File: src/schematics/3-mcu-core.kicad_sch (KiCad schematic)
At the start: 42 parts, among them U301 PIC32CX1025SG41100T-I/E5X

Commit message: Further MCU elaboration and pin mapping.
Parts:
- added R12, R13, R3??, R3ca-3cb, R3cb: ??Ω, restall-generic-resistors:nominal-0402-1005, symbol restall-generic-resistors:resistor
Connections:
- net SWCLK: now also U301.60 (PC20)
- net SWDIO: now also U301.61 (PC21)
- net TFT_SEL: now also U301.41 (PC11)
- net ~{RESET}: now also U301.58 (PC18)
- net ~{SDCARD_BUSYLED}: now also U301.81 (PB25); no longer CONN5.2 (P2)
- net ~{TFT_RESET}: now also U301.40 (PC10)
- net MSF_OUT_{+}: now reaches U301.15 (PB08)
- net MSF_OUT_{-}: now reaches U301.16 (PB09)
- net AMP_IN: now reaches U301.18 (PA05)
- net SHCP: now reaches U301.21 (PC05)
- net STCP: now reaches U301.22 (PC06)
- net DS: now reaches U301.23 (PC07)
- net at U301.26 (PA08): now also R3ca-3cb.2
- net at U301.27 (PA09): now also R12.2
- net at U301.28 (PA10): now also R13.2
- net at U301.29 (PA11): now also R3cb.2
- net AMP_EN: now reaches U301.3 (PC00)
- net at U301.32 (PB10): now also R3??.2
- net ~{SS}: now reaches U301.33 (PB11)
- net TFT_TEAR0: now reaches U301.34 (PB12)
- net TFT_TEAR1: now reaches U301.35 (PB13)
- net TFT_TP_INT0: now reaches U301.36 (PB14)
- net TFT_TP_INT1: now reaches U301.37 (PB15)
- net MSF_REC_EN: now reaches U301.4 (PC01)
- net D_{-}: now reaches U301.74 (PA24)
- net D_{+}: now reaches U301.75 (PA25)
- new net DATA0: R3ca-3cb.1
- new net DATA1: R12.1
- new net DATA2: R13.1
- new net DATA3: R3cb.1
- new net SCK: R3??.1
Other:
- note added: "TODO: BUSYLED WANTS A MOSFET / BJT - LESS INSTANTANEOUS CURRENT FLOWING THROUGH MCU'S VSS."
- note added: "TODO: CAPACITOR(S) ?"
- note added: "TODO: FIG9.4 / P28 of PIC32 Troubleshooting - example of SWD ESD / pull-ups"
- note added: "TODO: GND, PREFERABLY - OR GND THROUGH R. KEEPS NOISE FROM OSCILLATOR (JITTER). STATIC DIGITAL I/O FINE TOO - LIKE USB_SUSPEND MAYBE ?"
- note added: "TODO: NEED PULL-UPS OR ANYTHING ON THE DEBUG PINS ? SWCLK NEEDS 1k PULL-UP POSSIBLY ESD PROTECTION AT ALL CONNECTORS"
- note added: "TODO: P5-P20 are INPUT ONLY"
- note added: "TODO: PB0-3 = gnd ideally"
- note added: "TODO: PULL-UPS OR PULL-DOWNS ON TFT_TEAR* AND TFT_INT* ? IN CASE THE CONNECTOR POPS OUT. MAYBE JUST USE INTERNAL ONES ?"
- note added: "TODO: SPI - SERCOM: PAD1 IS CLK PAD2 IS SS (ONLY USED IN SLAVE MODE - SO TIE THIS TO ~{RESET}) PAD0 OR PAD3 IS DATA OUT PAD3 OR PAD0 IS DATA IN UART: TX=PAD0, RX=PAD1(OR SCK IF SYNC, THEN RX=PAD0), CTS=PAD3, RTS=PAD2"
- note added: "TODO: SPI.~{SS} NEEDS A PULL-UP TO VDD - BUT IT ALREADY WILL HAVE ONE SINCE IT'S SHARED WITH THE RESET..."
- note added: "TODO: SWCLK / SWDIO - NEED SERIES TERMINATORS..."
- note added: "TODO: THE SPI.~{SS} PAD IS REQUIRED BY THE BC805M SLAVE - THIS MEANS THE RESET PIN MUST BE USED AS A GPIO."
- note added: "TODO: THESE NETS NEED SUPPLIES / CIRCUITRY"
- note added: "TODO: UART RX FOR IR RECEIVER"
- note added: "TODO: series terminators, subtract 4.5ohms for switch resistance"
- note added: "TODO: ~{RESET} NEEDS TO BE SHARED...WON'T BE A DIRECT DEBUG BUS CONNECTION. WILL ALSO WANT A PULL-UP, CAPACITOR, ETC. A PUSH-BUTTON ALSO (BUTTON IN ROOT SCHEMATIC; ADD HIERARCHY PIN)"
- note added: "x BLE_DEBUG = 2 pins + 2o x MSF GAIN CONTROL = 3 pins + 3o x MSF POWER = 1 pin + 1o USB POWER FAULT = 1 pin + USB FUSB INT = 1 pin + USB BC DETECT = 3 pins + USB SUSPEND OUTPUT = 1 pin + 1o SD CARD POWER = 1 pin + 1o x AUDIO POWER = 1 pin + 1o HUMIDITY = 1 pin (optionally 2 pins) + PROXIMITY = 2 pins + PRESSURE = 1 pin = 19 pins ! (9 outputs)"
- note removed: "TODO: IR UART (CHECK SERCOM PINS !) MAYBE EVEN ANOTHER PERIPHERAL LIKE TCC ? AND THEN THIS SERCOM CAN BE USED FOR THE BC805M SWD. SERCOM5 (P99 & P100) MIGHT BE BETTER FOR IR LED. ALSO CONSIDER 'WAKE UP' - SERCOM NEEDS CLOCKING TO OPERATE IN SLEEP (TOO MUCH CURRENT FOR USB SUSPEND)"
- note removed: "TODO: NEED PULL-UPS OR ANYTHING ON THE DEBUG PINS ?"
- note removed: "TODO: SPEAKER"
- note removed: "TODO: SPI - SERCOM: PAD1 IS CLK PAD2 IS SS PAD0 OR PAD3 IS DATA OUT PAD3 OR PAD0 IS DATA IN UART: TX, RX, CTS, RTS"
- note removed: "TODO: SPI.~{SS} NEEDS A PULL-UP TO VDD"
- note removed: "TODO: ~{RESET} NEEDS TO BE SHARED...WON'T BE A DIRECT DEBUG BUS CONNECTION."
- moved on the sheet: C14, C15, C16, C17, C301, C302, R1, R2, R301, XTAL301, XTAL302, XTAL303

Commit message: Further elaboration of the design, particularly around the power budget.  It's clear that the USB Suspend current of 2.5mA won't be met, mainly due to the DPS1133 power switch's quiescent current.  This is a nice part worth keeping though as it contains OVP, OCP and reverse voltage protection all in one, up to 24V maximum input.
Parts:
- added Q1: MMBT3904, restall-manufacturer-diodes-inc:SOT-23, symbol restall-manufacturer-diodes-inc:MMBT3904
- added R2: 3.3kΩ, restall-generic-resistors:nominal-0402-1005, symbol restall-generic-resistors:resistor
- added R304, R305: 1.8kΩ, restall-generic-resistors:nominal-0402-1005, symbol restall-generic-resistors:resistor
- renumbered R1 to R302, R2 to R303
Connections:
- net GND: now also Q1.2 (E)
- net MCU_V{DD}: now also R304.1, R305.1
- net ~{SDCARD_BUSYLED}: now also Q1.3 (C); no longer U301.81 (PB25)
- net SDA: now reaches U301.72 (PA22)
- net SDA: now also R304.2
- net SCL: now reaches U301.73 (PA23)
- net SCL: now also R305.2
- new net: R2.1, U301.81 (PB25)
- new net: Q1.1 (B), R2.2
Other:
- note added: "Fast-Mode I^{2}C (400kHz)"
- note removed: "I2C SDA (P72 / PAD0) AND SCL (P73 / PAD1)"
- note removed: "TODO: BUSYLED WANTS A MOSFET / BJT - LESS INSTANTANEOUS CURRENT FLOWING THROUGH MCU'S VSS."

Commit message: Elaboration of the top-level schematicd.
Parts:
- added R3bb1, R3xx: ??Ω, restall-generic-resistors:nominal-0402-1005, symbol restall-generic-resistors:resistor
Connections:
- net SWCLK: now also R3bb1.2; no longer U301.60 (PC20)
- net SWDIO: now also R3xx.2; no longer U301.61 (PC21)
- net CD renamed ~{CD}
- net MSF_REC_EN renamed MSF_RCV_EN
- net WP renamed ~{WP}
- new net: R3bb1.1, U301.60 (PC20)
- new net: R3xx.1, U301.61 (PC21)
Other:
- note added: "R3??-??"
- note added: "TODO: ABOUT 330 ohms - less about Z matching, more about isolating from connector / debugger"
- note added: "TODO: ALREADY GOT THE BACKLIGHT SOMEWHERE ?"
- note added: "TODO: NOTE ABOUT ALL R AND C BEING 0402 UNLESS SPECIFIED. ALSO ALL R THICK FILM 1% 100ppm. ALSO ALL C MLCC +/- 10% X5R 16V."
- note added: "TODO: RESET NEEDS TO BE: MCU -> SERIES R -> R (PULL-UP) AND C TO GND -> BUS Verify signal levels at BC805M side. Verify rise time for when using the pin as ~{SPI.SS}."
- note removed: "TODO: NOTE ABOUT ALL R AND C BEING 0402 UNLESS SPECIFIED. ALSO ALL R THICK FILM 1% 100ppm. ALSO ALL C MLCC +/- 10% X7R 10V."
- note removed: "TODO: SWCLK / SWDIO - NEED SERIES TERMINATORS..."

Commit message: Further elaboration of the design and schematics, mainly power supply calculations.
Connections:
- net MCU_V{DD} renamed CORE_VDD_{+3.3V}
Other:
- note added: "TODO: NOTE ABOUT ALL R AND C BEING 0402 UNLESS SPECIFIED. ALSO ALL R THICK FILM 1% 100ppm. ALSO ALL C MLCC +/- 10% X5R 10V."
- note removed: "TODO: NOTE ABOUT ALL R AND C BEING 0402 UNLESS SPECIFIED. ALSO ALL R THICK FILM 1% 100ppm. ALSO ALL C MLCC +/- 10% X5R 16V."
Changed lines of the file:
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@@
     (effects (font (size 1.27 1.27)) (justify left bottom))
   )
-  (text "TODO: NOTE ABOUT ALL R AND C BEING 0402 UNLESS SPECIFIED.\nALSO ALL R THICK FILM 1% 100ppm.\nALSO ALL C MLCC +/- 10% X5R 16V."
+  (text "TODO: NOTE ABOUT ALL R AND C BEING 0402 UNLESS SPECIFIED.\nALSO ALL R THICK FILM 1% 100ppm.\nALSO ALL C MLCC +/- 10% X5R 10V."
     (at 309.372 261.874 0)
     (effects (font (size 1.27 1.27)) (justify left bottom))
@@
     (effects (font (size 1.27 1.27)) (justify right))
   )
+  (hierarchical_label "CORE_VDD_MODE" (shape output) (at 305.054 228.854 0) (fields_autoplaced)
+    (effects (font (size 1.27 1.27)) (justify left))
+  )
   (hierarchical_label "{MCU_DEBUG}" (shape bidirectional) (at 137.16 86.36 180) (fields_autoplaced)
     (effects (font (size 1.27 1.27)) (justify right))
@@
     (effects (font (size 1.27 1.27)) (justify left))
   )
-  (hierarchical_label "MCU_V{DD}" (shape output) (at 355.6 81.28 0) (fields_autoplaced)
+  (hierarchical_label "CORE_VDD_{+3.3V}" (shape input) (at 355.6 81.28 0) (fields_autoplaced)
     (effects (font (size 1.27 1.27)) (justify left))
   )
@@
           (reference "R2") (unit 1)
         )
-        (path "/56d623d3-22db-4d43-a9d9-e6bb4bb68946"
-          (reference "R001") (unit 1)
-        )
-        (path "/56d623d3-22db-4d43-a9d9-e6bb4bb68946/f496ae57-4ed4-47d4-8c97-f77f6741aea7"
-          (reference "R501") (unit 1)
-        )
       )
     )
@@
           (reference "R304") (unit 1)
         )
-        (path "/56d623d3-22db-4d43-a9d9-e6bb4bb68946"
-          (reference "R001") (unit 1)
-        )
-        (path "/56d623d3-22db-4d43-a9d9-e6bb4bb68946/f496ae57-4ed4-47d4-8c97-f77f6741aea7"
-          (reference "R501") (unit 1)
-        )
       )
     )
@@
           (reference "R305") (unit 1)
         )
-        (path "/56d623d3-22db-4d43-a9d9-e6bb4bb68946"
-          (reference "R001") (unit 1)
-        )
-        (path "/56d623d3-22db-4d43-a9d9-e6bb4bb68946/f496ae57-4ed4-47d4-8c97-f77f6741aea7"
-          (reference "R501") (unit 1)
-        )
-      )
+      )

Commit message: Started to draw the USB / power input module.
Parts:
- removed FB1: >600R @ 100MHz, symbol restall-generic-inductors:ferrite-bead
- added FB301: WLBD2012HCU601TH, restall-manufacturer-walsin:WLBD2012, symbol restall-manufacturer-walsin:WLBD2012HCU601TH
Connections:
- net CORE_VDD_{+3.3V}: now also FB301.1 (P1)
- net MCU_AV_{DD}: now also FB301.2 (P2)
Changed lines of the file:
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@@
     (stroke (width 0) (type default))
   )
+  (wire (pts (xy 71.12 101.6) (xy 76.2 101.6))
+    (stroke (width 0) (type default))
+  )
   (wire (pts (xy 132.08 238.76) (xy 139.7 238.76))
     (stroke (width 0) (type default))
@@
     (stroke (width 0) (type default))
   )
-  (wire (pts (xy 71.12 101.6) (xy 76.2 101.6))
-    (stroke (width 0) (type default))
-  )
   (wire (pts (xy 219.71 144.78) (xy 227.33 144.78))
     (stroke (width 0) (type default))
@@
     )
   )
-  (symbol (lib_id "restall-generic-inductors:ferrite-bead") (at 78.74 101.6 90) (unit 1)
-    (in_bom yes) (on_board yes) (dnp no) (fields_autoplaced)
-    (property "Reference" "FB1" (at 78.7019 95.7539 90)
-      (effects (font (size 1.27 1.27)))
-    )
-    (property "Value" ">600R @ 100MHz" (at 78.7019 98.1781 90)
-      (effects (font (size 1.27 1.27)))
-    )
-    (property "Footprint" "" (at 78.74 103.378 90)
-      (effects (font (size 1.27 1.27)) (justify left) hide)
-    )
-    (property "Datasheet" "~" (at 78.74 101.6 0)
-      (effects (font (size 1.27 1.27)) (justify left) hide)
-    )
-    (property "Label" "??A, ??mΩ @ DC, ??Ω±??% @ 100MHz" (at 81.788 99.568 0)
-      (effects (font (size 1.27 1.27)) (justify left) hide)
-    )
-    (property "I_{MAX}" "??A" (at 83.82 99.568 0)
-      (effects (font (size 1.27 1.27)) (justify left) hide)
-    )
-    (property "DCR" "??mΩ" (at 85.852 99.568 0)
-      (effects (font (size 1.27 1.27)) (justify left) hide)
-    )
-    (property "Impedance" "??Ω @ 100MHz" (at 87.884 99.568 0)
-      (effects (font (size 1.27 1.27)) (justify left) hide)
-    )
-    (property "Tolerance" "±??%" (at 89.916 99.568 0)
-      (effects (font (size 1.27 1.27)) (justify left) hide)
-    )
-    (property "Package" "" (at 78.74 101.6 0)
-      (effects (font (size 1.27 1.27)) (justify left) hide)
-    )
-    (property "Manufacturer" "" (at 78.74 101.6 0)
-      (effects (font (size 1.27 1.27)) (justify left) hide)
-    )
-    (property "ManufacturerPartNumber" "" (at 78.74 101.6 0)
-      (effects (font (size 1.27 1.27)) (justify left) hide)
-    )
-    (property "Manufacturer2" "" (at 78.74 101.6 0)
-      (effects (font (size 1.27 1.27)) (justify left) hide)
-    )
-    (property "Manufacturer2PartNumber" "" (at 78.74 101.6 0)
-      (effects (font (size 1.27 1.27)) (justify left) hide)
-    )
-    (pin "1")
-    (pin "2")
-    (instances
-      (project "msf-owl-clock"
-        (path "/56d623d3-22db-4d43-a9d9-e6bb4bb68946/cc278a5b-e802-444a-81ef-f38d11985404"
-          (reference "FB1") (unit 1)
-        )
-      )
-    )
-  )
   (symbol (lib_id "restall-generic-resistors:resistor") (at 154.94 208.28 180) (unit 1)
     (in_bom yes) (on_board yes) (dnp no)
@@
         )
       )
+    )
+  )
+  (symbol (lib_id "restall-manufacturer-walsin:WLBD2012HCU601TH") (at 78.74 101.6 90) (unit 1)
+    (in_bom yes) (on_board yes) (dnp no)
+    (property "Reference" "FB301" (at 66.294 94.742 90)
+      (effects (font (size 1.27 1.27)) (justify right))
+    )
+    (property "Value" "WLBD2012HCU601TH" (at 66.294 96.6582 90)
+      (effects (font (size 1.27 1.27)) (justify right))
+    )
+    (property "Footprint" "restall-manufacturer-walsin:WLBD2012" (at 78.74 103.378 90)
+      (effects (font (size 1.27 1.27)) (justify right) hide)
+    )
+    (property "Datasheet" "https://www.passivecomponent.com/wp-content/uploads/inductor/WLBD1005-4532_HC.pdf" (at 96.266 99.568 0)
+      (effects (font (size 1.27 1.27)) (justify left) hide)
+    )
+    (property "Label" "2A, 90mΩ @ DC, 600Ω±25% @ 100MHz" (at 66.294 98.552 90)
+      (effects (font (size 1.27 1.27)) (justify right))
+    )
+    (property "DCR" "90mΩ" (at 88.138 99.568 0)
+      (effects (font (size 1.27 1.27)) (justify left) hide)
+    )
+    (property "I_{MAX}" "2A" (at 86.106 99.568 0)
+      (effects (font (size 1.27 1.27)) (justify left) hide)
+    )
+    (property "Impedance" "600Ω @ 100MHz" (at 90.17 99.568 0)
+      (effects (font (size 1.27 1.27)) (justify left) hide)
+    )
+    (property "Tolerance" "±25%" (at 92.202 99.822 0)
+      (effects (font (size 1.27 1.27)) (justify left) hide)
+    )
+    (property "Manufacturer" "Walsin Technology" (at 94.234 99.568 0)
+      (effects (font (size 1.27 1.27)) (justify left) hide)
+    )
+    (property "ManufacturerPartNumber" "WLBD2012HCU601TH" (at 82.042 99.568 0)
+      (effects (font (size 1.27 1.27)) (justify left) hide)
+    )
+    (pin "1")
+    (pin "2")
+    (instances
+      (project "msf-owl-clock"
+        (path "/56d623d3-22db-4d43-a9d9-e6bb4bb68946/cc278a5b-e802-444a-81ef-f38d11985404"
+          (reference "FB301") (unit 1)
+        )
+      )

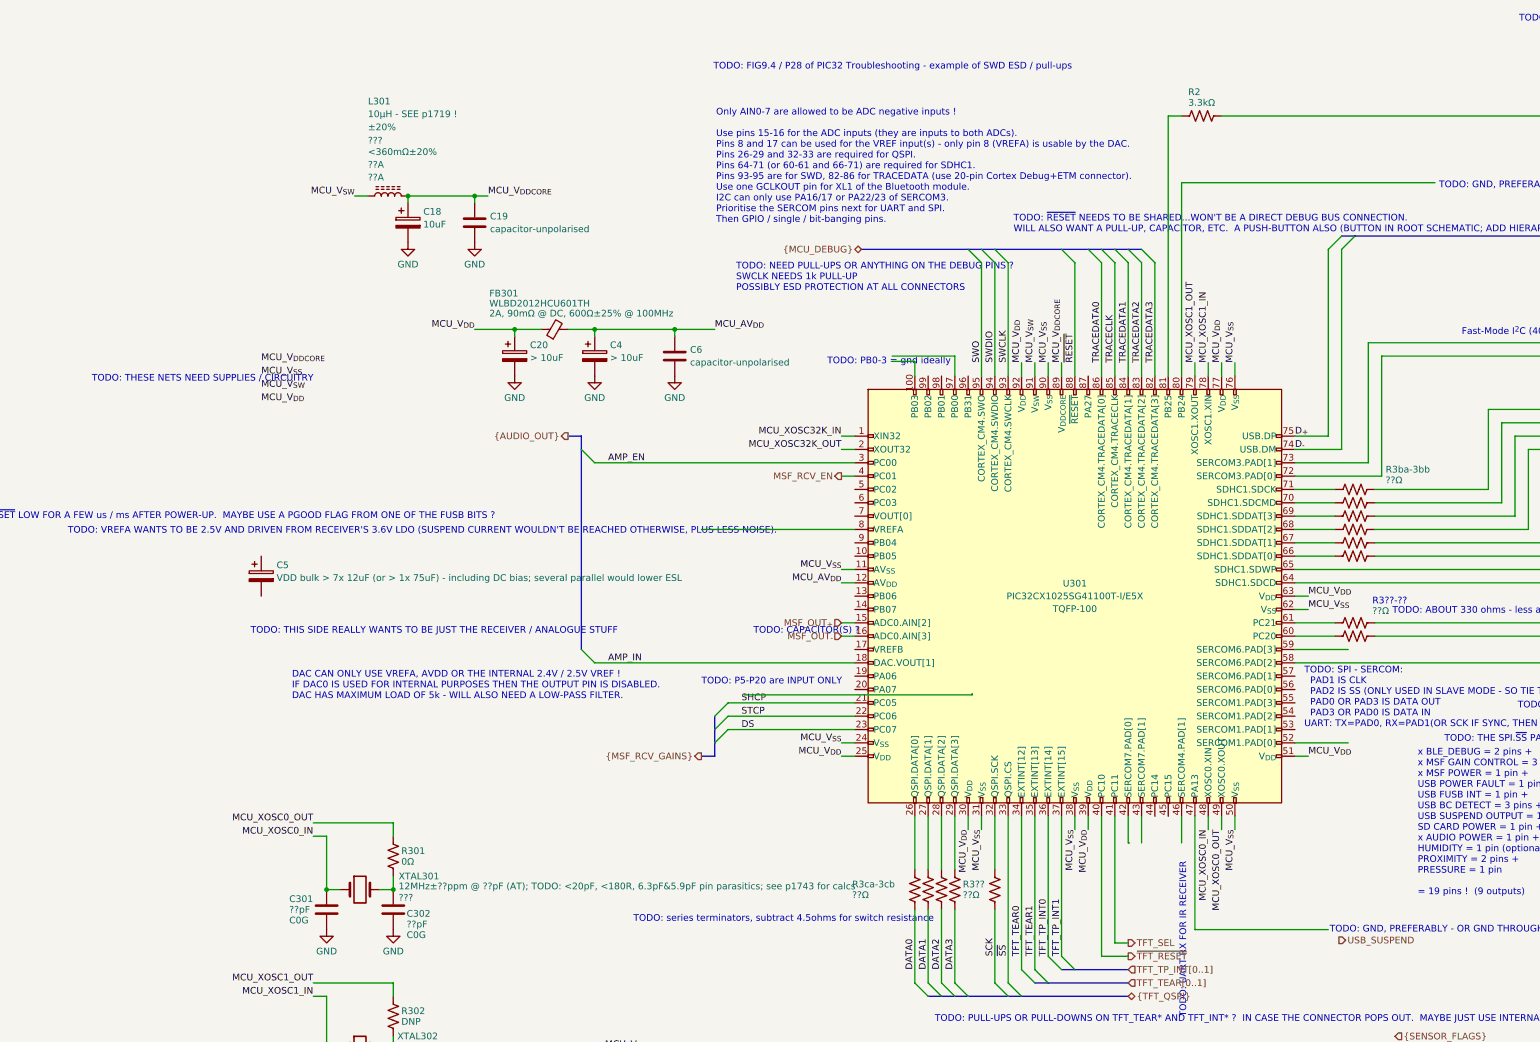
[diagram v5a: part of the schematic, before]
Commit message: Further elaboration of the USB / Power schematic.
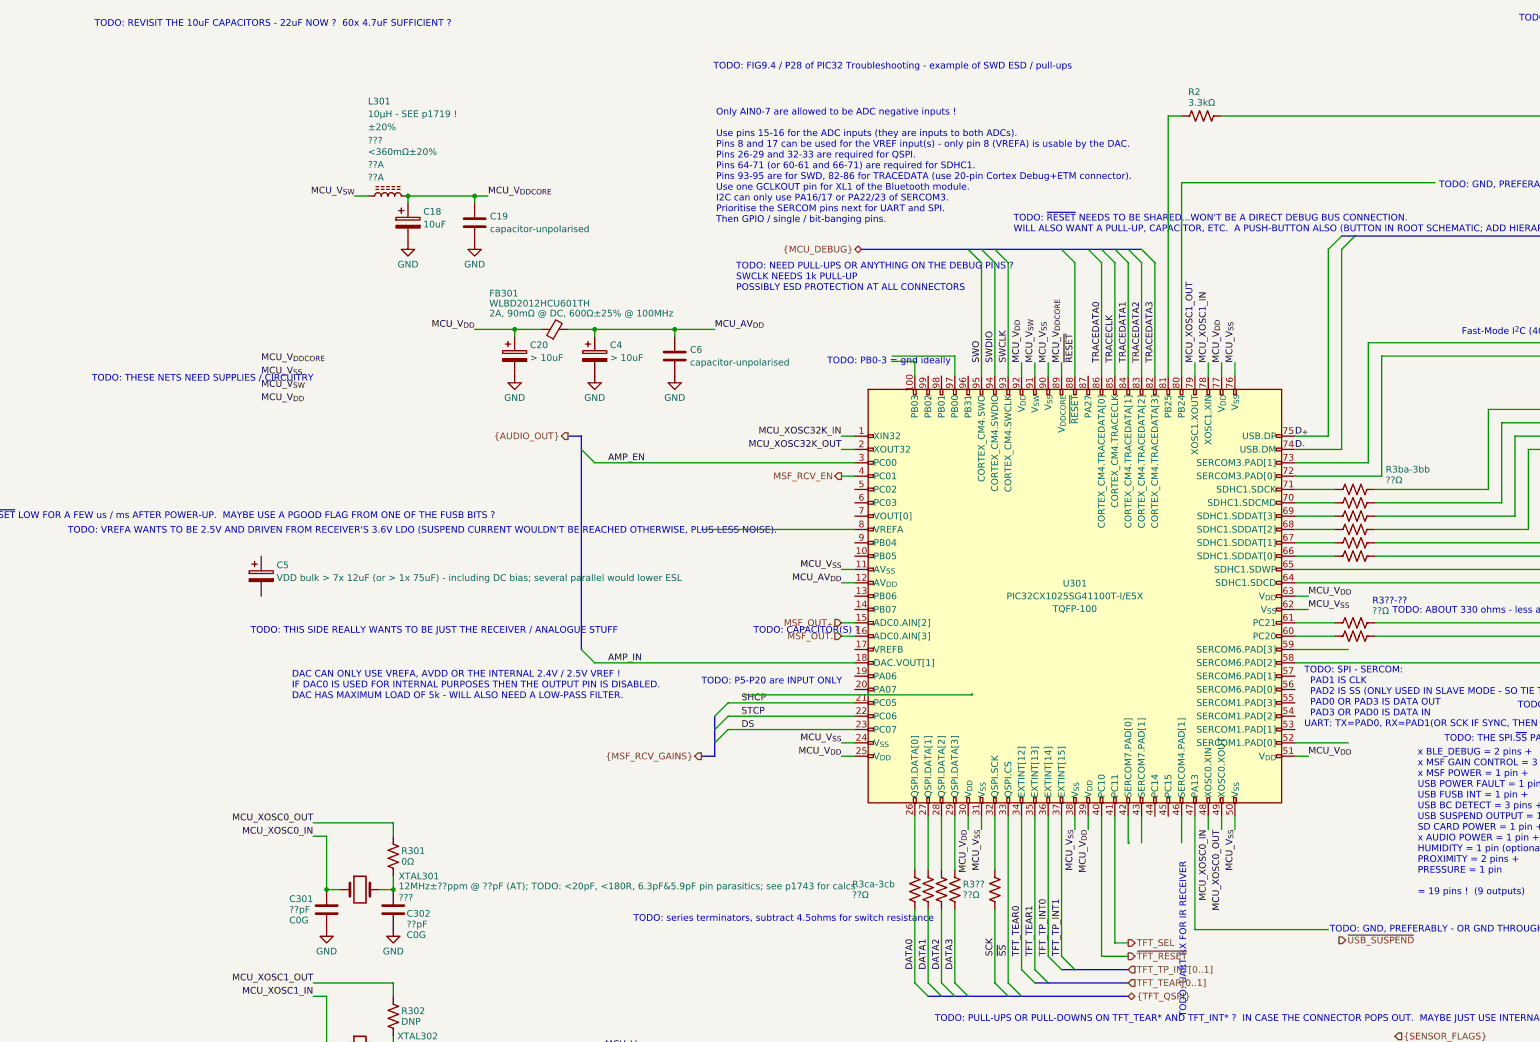
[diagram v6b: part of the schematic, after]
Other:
- note added: "TODO: REVISIT THE 10uF CAPACITORS - 22uF NOW ? 60x 4.7uF SUFFICIENT ?"
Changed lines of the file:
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@@
+    (effects (font (size 1.27 1.27)) (justify left bottom))
+  )
+  (text "TODO: REVISIT THE 10uF CAPACITORS - 22uF NOW ?  60x 4.7uF SUFFICIENT ?"
+    (at -8.89 44.196 0)
     (effects (font (size 1.27 1.27)) (justify left bottom))
   )
@@
     (effects (font (size 1.27 1.27)) (justify left))
   )
-  (hierarchical_label "USB_SUSPEND" (shape output) (at 228.092 217.932 0) (fields_autoplaced)
-    (effects (font (size 1.27 1.27)) (justify left))
-  )
+  (hierarchical_label "~{USB_SUSPEND}" (shape output) (at 228.092 217.932 0) (fields_autoplaced)
+    (effects (font (size 1.27 1.27)) (justify left))
+  )
